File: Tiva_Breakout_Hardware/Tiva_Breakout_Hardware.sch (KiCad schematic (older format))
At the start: 6 parts, among them U1 TM4C129E_Launchpad

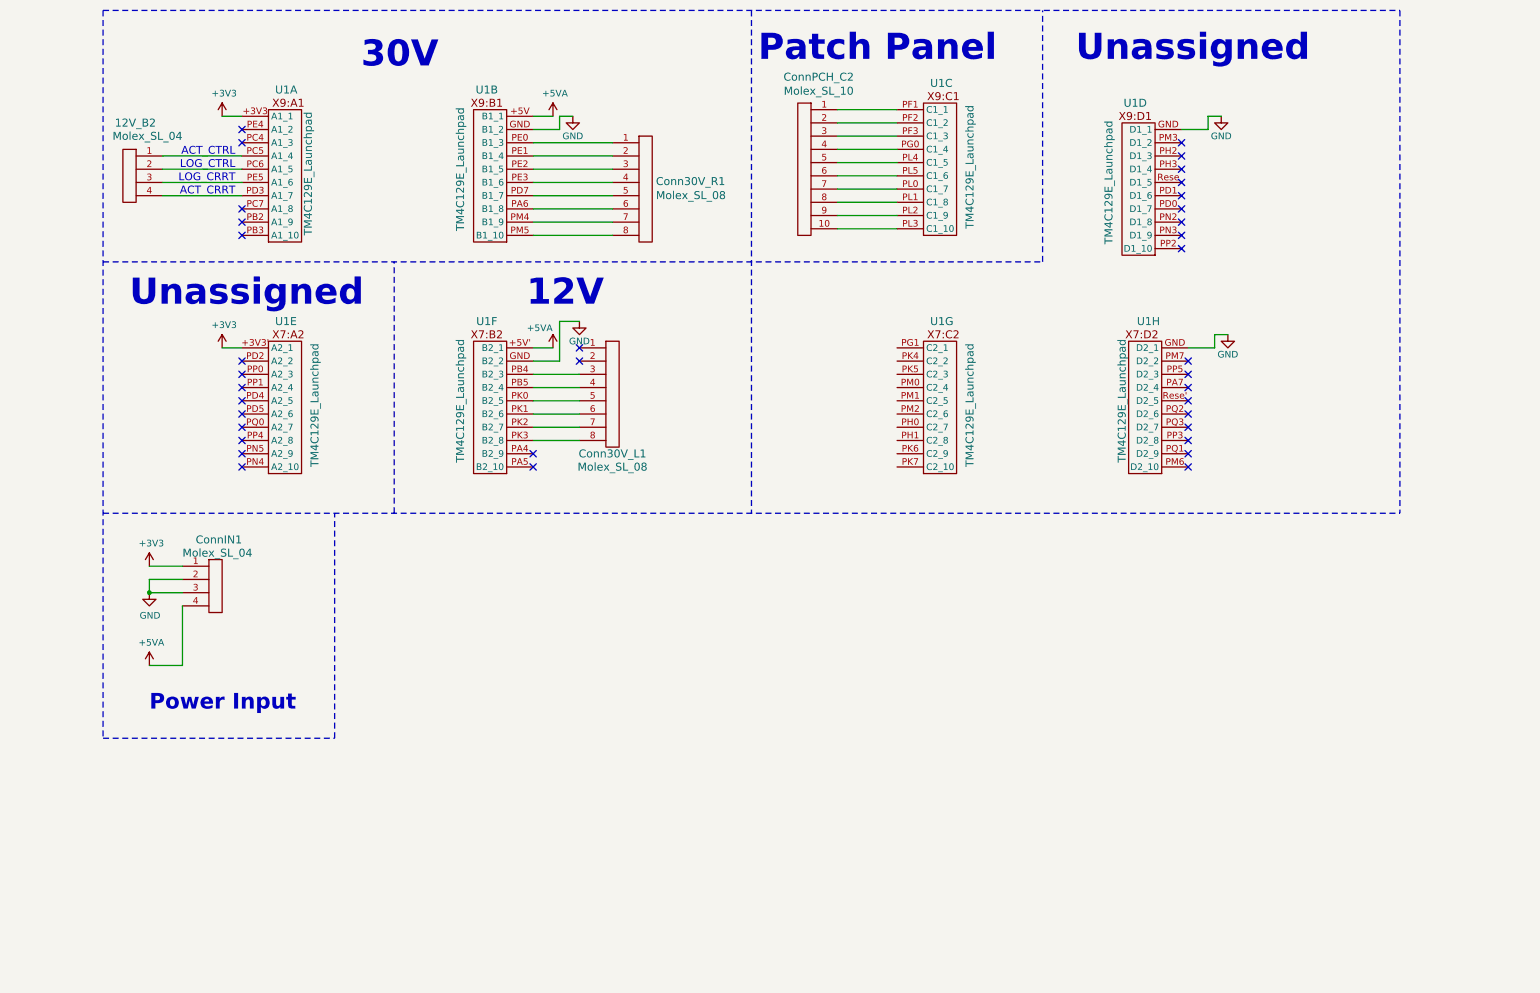
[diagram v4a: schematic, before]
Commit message: Corrected schematic to match 30V board
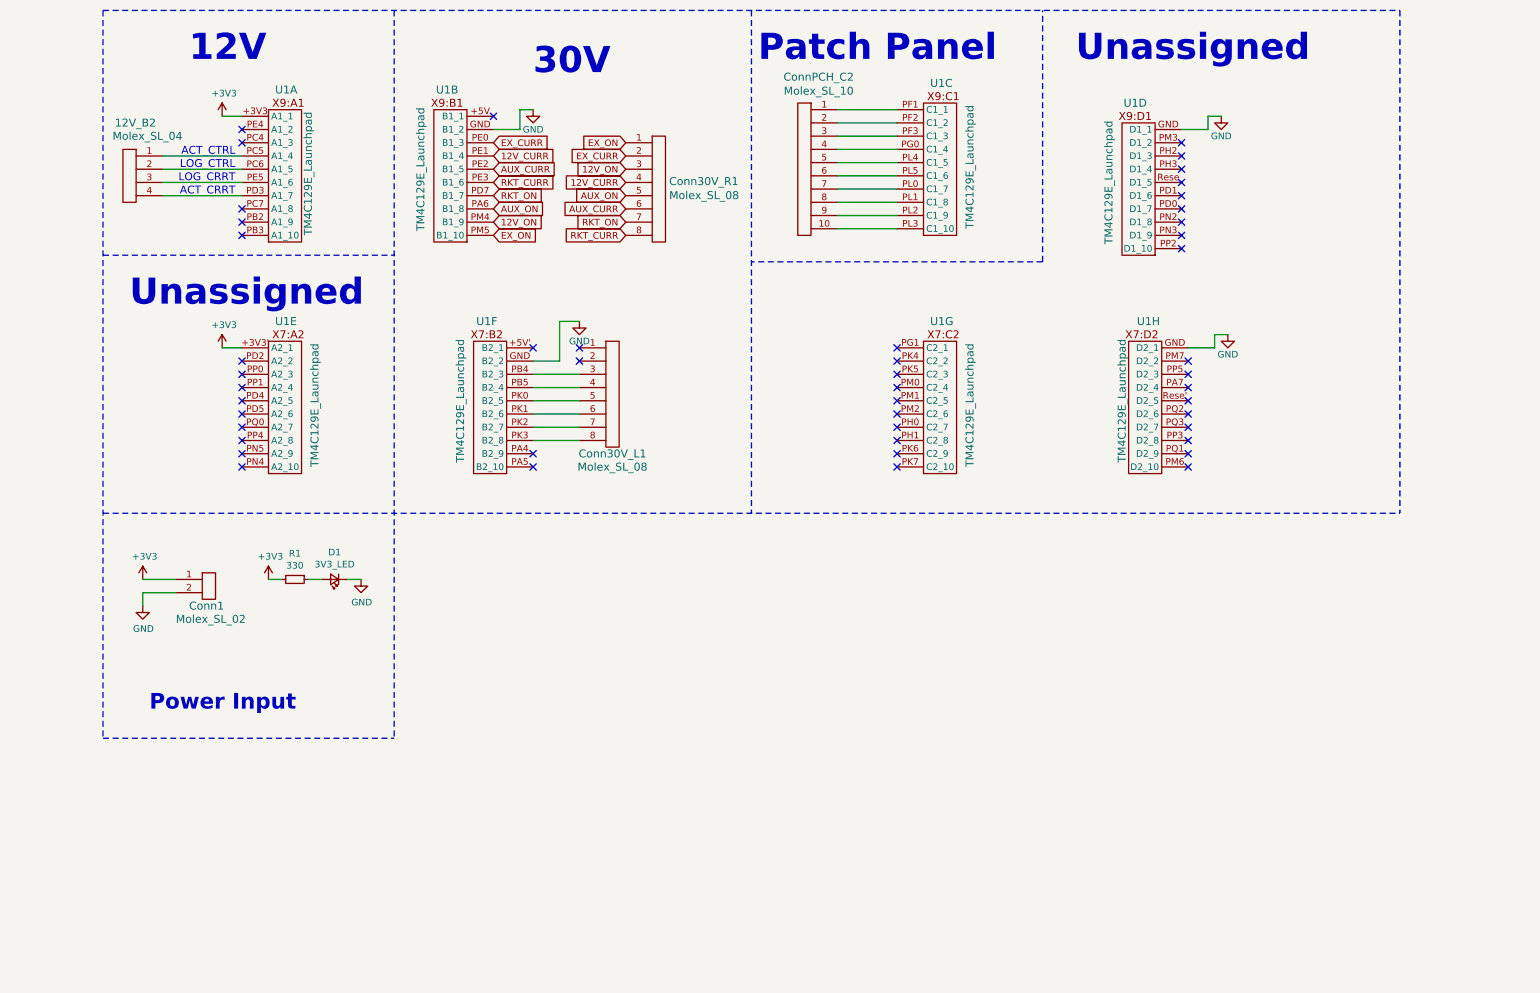
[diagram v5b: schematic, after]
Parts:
- removed ConnIN1: Molex_SL_04, MRDT_Connectors:MOLEX_SL_04_Horizontal, symbol Tiva_Breakout_Hardware-rescue:Molex_SL_04-MRDT_Connectors
- added Conn1: Molex_SL_02, MRDT_Connectors:MOLEX_SL_02_Horizontal, symbol MRDT_Connectors:Molex_SL_02
- added D1: 3V3_LED, LED_SMD:LED_0603_1608Metric_Pad1.05x0.95mm_HandSolder, symbol Device:LED_Small
- added R1: 330, Resistor_SMD:R_0603_1608Metric_Pad1.05x0.95mm_HandSolder, symbol Device:R_Small
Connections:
- net +3V3: now also Conn1.1, R1.2
- net GND: now also Conn1.2, D1.1 (K)
- net AUX_CURR: now reaches Conn30V_R1.6
- net AUX_CURR: now also U1.PE2 (B1_5); no longer U1.PA6 (B1_8)
- net AUX_ON: now reaches Conn30V_R1.5
- net AUX_ON: now also U1.PA6 (B1_8); no longer U1.PD7 (B1_7)
- net EX_CURR: now reaches U1.PE0 (B1_3)
- net EX_CURR: now also Conn30V_R1.2; no longer Conn30V_R1.1
- net 12V_CURR: now reaches U1.PE1 (B1_4)
- net 12V_CURR: now also Conn30V_R1.4; no longer Conn30V_R1.2
- net 12V_ON: now reaches Conn30V_R1.3
- net 12V_ON: now also U1.PM4 (B1_9); no longer U1.PE2 (B1_5)
- net RKT_CURR: now reaches U1.PE3 (B1_6)
- net RKT_CURR: now also Conn30V_R1.8; no longer Conn30V_R1.4
- net RKT_ON: now reaches Conn30V_R1.7
- net RKT_ON: now also U1.PD7 (B1_7); no longer U1.PM4 (B1_9)
- net EX_ON: now reaches U1.PM5 (B1_10)
- net EX_ON: now also Conn30V_R1.1; no longer Conn30V_R1.8
- net +5VA: no longer names the net of U1.+5V (B1_1)
- net +5VA: no longer U1.+5V' (B2_1)
- new net: D1.2 (A), R1.1
- no-connect marks 36 -> 48
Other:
- moved on the sheet: Conn30V_R1, U1B
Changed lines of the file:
@@
 L power:GND #PWR0101
 U 1 1 5D91D7D5
-P 800 4850
-F 0 "#PWR0101" H 800 4600 50  0001 C CNN
-F 1 "GND" H 805 4677 50  0000 C CNN
-F 2 "" H 800 4850 50  0001 C CNN
-F 3 "" H 800 4850 50  0001 C CNN
-	1    800  4850
-	1    0    0    -1
-$EndComp
-Wire Wire Line
-	1050 4850 800  4850
-Wire Wire Line
-	800  4850 800  4750
-Wire Wire Line
-	800  4750 1050 4750
-Connection ~ 800  4850
-$Comp
-L power:+5VA #PWR0102
-U 1 1 5D91FD34
-P 800 5400
-F 0 "#PWR0102" H 800 5250 50  0001 C CNN
-F 1 "+5VA" H 815 5573 50  0000 C CNN
-F 2 "" H 800 5400 50  0001 C CNN
-F 3 "" H 800 5400 50  0001 C CNN
-	1    800  5400
-	1    0    0    -1
-$EndComp
-Wire Wire Line
-	800  4650 1050 4650
+P 750 4950
+F 0 "#PWR0101" H 750 4700 50  0001 C CNN
+F 1 "GND" H 755 4777 50  0000 C CNN
+F 2 "" H 750 4950 50  0001 C CNN
+F 3 "" H 750 4950 50  0001 C CNN
+	1    750  4950
+	1    0    0    -1
+$EndComp
+Wire Wire Line
+	750  4950 750  4850
+Wire Wire Line
+	750  4850 1000 4850
 $Comp
 L power:+3V3 #PWR0103
 U 1 1 5D920B87
-P 800 4650
-F 0 "#PWR0103" H 800 4500 50  0001 C CNN
-F 1 "+3V3" H 815 4823 50  0000 C CNN
-F 2 "" H 800 4650 50  0001 C CNN
-F 3 "" H 800 4650 50  0001 C CNN
-	1    800  4650
-	1    0    0    -1
-$EndComp
-Wire Wire Line
-	1050 4950 1050 5400
-Wire Wire Line
-	1050 5400 800  5400
-Wire Notes Line
-	2200 5950 2200 4250
+P 750 4750
+F 0 "#PWR0103" H 750 4600 50  0001 C CNN
+F 1 "+3V3" H 765 4923 50  0000 C CNN
+F 2 "" H 750 4750 50  0001 C CNN
+F 3 "" H 750 4750 50  0001 C CNN
+	1    750  4750
+	1    0    0    -1
+$EndComp
 Text Notes 800  5750 0    118  ~ 24
 Power Input
 NoConn ~ 8650 3400
-$Comp
-L power:+5VA #PWR0104
-U 1 1 5D92EDF1
-P 3850 3000
-F 0 "#PWR0104" H 3850 2850 50  0001 C CNN
-F 1 "+5VA" H 3750 3150 50  0000 C CNN
-F 2 "" H 3850 3000 50  0001 C CNN
-F 3 "" H 3850 3000 50  0001 C CNN
-	1    3850 3000
-	1    0    0    -1
-$EndComp
-Wire Wire Line
-	3700 3000 3850 3000
 $Comp
 L power:+3V3 #PWR0105
@@
 	1350 1250 1500 1250
 Wire Wire Line
-	3900 1250 4000 1250
-Wire Wire Line
-	3900 1350 3900 1250
-Wire Wire Line
-	3700 1350 3900 1350
+	3600 1200 3700 1200
+Wire Wire Line
+	3400 1350 3600 1350
 $Comp
 L power:GND #PWR0107
 U 1 1 5D932528
-P 4000 1250
-F 0 "#PWR0107" H 4000 1000 50  0001 C CNN
-F 1 "GND" H 4000 1100 50  0000 C CNN
-F 2 "" H 4000 1250 50  0001 C CNN
-F 3 "" H 4000 1250 50  0001 C CNN
-	1    4000 1250
-	1    0    0    -1
-$EndComp
-Wire Wire Line
-	3700 1250 3850 1250
-$Comp
-L power:+5VA #PWR0108
-U 1 1 5D92E21C
-P 3850 1250
-F 0 "#PWR0108" H 3850 1100 50  0001 C CNN
-F 1 "+5VA" H 3865 1423 50  0000 C CNN
-F 2 "" H 3850 1250 50  0001 C CNN
-F 3 "" H 3850 1250 50  0001 C CNN
-	1    3850 1250
+P 3700 1200
+F 0 "#PWR0107" H 3700 950 50  0001 C CNN
+F 1 "GND" H 3700 1050 50  0000 C CNN
+F 2 "" H 3700 1200 50  0001 C CNN
+F 3 "" H 3700 1200 50  0001 C CNN
+	1    3700 1200
 	1    0    0    -1
 $EndComp
@@
 	8850 2900 8950 2900
 Wire Wire Line
-	3700 1450 4300 1450
-Wire Wire Line
-	3700 1550 4300 1550
-Wire Wire Line
-	3700 1650 4300 1650
-Wire Wire Line
-	3700 1750 4300 1750
-Wire Wire Line
-	3700 1850 4300 1850
-Wire Wire Line
-	3700 1950 4300 1950
-Wire Wire Line
 	6000 1200 6450 1200
 Wire Wire Line
@@
 L Tiva_Breakout_Hardware-rescue:TM4C129E_Launchpad-MRDT_Shields U1
 U 2 1 5D8F2703
-P 3500 2200
-F 0 "U1" H 3650 3350 60  0000 C CNN
-F 1 "TM4C129E_Launchpad" V 3850 2750 60  0000 C CNN
-F 2 "MRDT_Shields:Tiva_Breakout" H 3500 2200 60  0001 C CNN
-F 3 "" H 3500 2200 60  0001 C CNN
-	2    3500 2200
+P 3200 2200
+F 0 "U1" H 3350 3350 60  0000 C CNN
+F 1 "TM4C129E_Launchpad" V 3550 2750 60  0000 C CNN
+F 2 "MRDT_Shields:Tiva_Breakout" H 3200 2200 60  0001 C CNN
+F 3 "" H 3200 2200 60  0001 C CNN
+	2    3200 2200
 	-1   0    0    -1
 $EndComp
@@
 	8    8450 3950
 	-1   0    0    -1
-$EndComp
-$Comp
-L Tiva_Breakout_Hardware-rescue:Molex_SL_04-MRDT_Connectors ConnIN1
-U 1 1 5D9064E6
-P 1250 5000
-F 0 "ConnIN1" H 1150 5550 60  0000 L CNN
-F 1 "Molex_SL_04" H 1050 5450 60  0000 L CNN
-F 2 "MRDT_Connectors:MOLEX_SL_04_Horizontal" H 1250 5000 60  0001 C CNN
-F 3 "" H 1250 5000 60  0001 C CNN
-	1    1250 5000
-	1    0    0    -1
 $EndComp
 $Comp
@@
 	-1   0    0    -1
 $EndComp
-Text Notes 2400 900  0    197  ~ 39
+Text Notes 3700 950  0    197  ~ 39
 30V
-Text Notes 3650 2700 0    197  ~ 39
+Text Notes 1100 850  0    197  ~ 39
 12V
 Wire Wire Line
@@
 Text Notes 5400 850  0    197  ~ 39
 Patch Panel
-Wire Notes Line
-	2650 4250 2650 2350
 Text Notes 650  2700 0    197  ~ 39
 Unassigned
 Wire Notes Line
 	450  4250 10250 4250
-Wire Notes Line
-	450  5950 2200 5950
 Wire Notes Line
 	450  450  450  5950
@@
 Wire Notes Line
 	7550 2350 7550 450
-Wire Notes Line
-	450  2350 7550 2350
 Text Notes 7800 850  0    197  ~ 39
 Unassigned
@@
 L MRDT_Connectors:Molex_SL_08 Conn30V_R1
 U 1 1 5DCE5C02
-P 4500 2200
-F 0 "Conn30V_R1" H 4628 2658 60  0000 L CNN
-F 1 "Molex_SL_08" H 4628 2552 60  0000 L CNN
-F 2 "MRDT_Connectors:MOLEX_SL_08_Horizontal" H 4500 2500 60  0001 C CNN
-F 3 "" H 4500 2500 60  0001 C CNN
-	1    4500 2200
-	1    0    0    -1
-$EndComp
-Wire Wire Line
-	3700 2050 4300 2050
-Wire Wire Line
-	3700 2150 4300 2150
+P 4600 2200
+F 0 "Conn30V_R1" H 4728 2658 60  0000 L CNN
+F 1 "Molex_SL_08" H 4728 2552 60  0000 L CNN
+F 2 "MRDT_Connectors:MOLEX_SL_08_Horizontal" H 4600 2500 60  0001 C CNN
+F 3 "" H 4600 2500 60  0001 C CNN
+	1    4600 2200
+	1    0    0    -1
+$EndComp
 NoConn ~ 4050 3000
 NoConn ~ 4050 3100
@@
 Wire Wire Line
 	900  1550 1500 1550
+$Comp
+L Device:R_Small R1
+U 1 1 5DD79B1A
+P 1900 4750
+F 0 "R1" V 1704 4750 50  0000 C CNN
+F 1 "330" V 1795 4750 50  0000 C CNN
+F 2 "Resistor_SMD:R_0603_1608Metric_Pad1.05x0.95mm_HandSolder" H 1900 4750 50  0001 C CNN
+F 3 "~" H 1900 4750 50  0001 C CNN
+	1    1900 4750
+	0    1    1    0
+$EndComp
+$Comp
+L Device:LED_Small D1
+U 1 1 5DD80F85
+P 2200 4750
+F 0 "D1" H 2200 4545 50  0000 C CNN
+F 1 "3V3_LED" H 2200 4636 50  0000 C CNN
+F 2 "LED_SMD:LED_0603_1608Metric_Pad1.05x0.95mm_HandSolder" V 2200 4750 50  0001 C CNN
+F 3 "~" V 2200 4750 50  0001 C CNN
+	1    2200 4750
+	-1   0    0    1
+$EndComp
+Wire Wire Line
+	2000 4750 2100 4750
+$Comp
+L power:GND #PWR0112
+U 1 1 5DD86867
+P 2400 4750
+F 0 "#PWR0112" H 2400 4500 50  0001 C CNN
+F 1 "GND" H 2405 4577 50  0000 C CNN
+F 2 "" H 2400 4750 50  0001 C CNN
+F 3 "" H 2400 4750 50  0001 C CNN
+	1    2400 4750
+	1    0    0    -1
+$EndComp
+Wire Wire Line
+	2300 4750 2400 4750
+$Comp
+L MRDT_Connectors:Molex_SL_02 Conn1
+U 1 1 5DD89AFE
+P 1200 4900
+F 0 "Conn1" H 1100 4850 60  0000 L CNN
+F 1 "Molex_SL_02" H 1000 4750 60  0000 L CNN
+F 2 "MRDT_Connectors:MOLEX_SL_02_Horizontal" H 1200 4800 60  0001 C CNN
+F 3 "" H 1200 4800 60  0001 C CNN
+	1    1200 4900
+	1    0    0    -1
+$EndComp
+NoConn ~ 3700 3000
+NoConn ~ 3400 1250
+NoConn ~ 6450 3000
+NoConn ~ 6450 3100
+NoConn ~ 6450 3200
+NoConn ~ 6450 3300
+NoConn ~ 6450 3400
+NoConn ~ 6450 3500
+NoConn ~ 6450 3600
+NoConn ~ 6450 3700
+NoConn ~ 6450 3800
+NoConn ~ 6450 3900
+Wire Notes Line
+	450  2300 2650 2300
+Wire Notes Line
+	7550 2350 5350 2350
+Wire Wire Line
+	3600 1200 3600 1350
+Text GLabel 3400 1450 2    50   Input ~ 0
+EX_CURR
+Text GLabel 3400 1550 2    50   Input ~ 0
+12V_CURR
+Text GLabel 3400 1650 2    50   Input ~ 0
+AUX_CURR
+Text GLabel 3400 1750 2    50   Input ~ 0
+RKT_CURR
+Text GLabel 3400 1850 2    50   Input ~ 0
+RKT_ON
+Text GLabel 3400 1950 2    50   Input ~ 0
+AUX_ON
+Text GLabel 3400 2050 2    50   Input ~ 0
+12V_ON
+Text GLabel 3400 2150 2    50   Input ~ 0
+EX_ON
+Text GLabel 4400 1450 0    50   Input ~ 0
+EX_ON
+Text GLabel 4400 1550 0    50   Input ~ 0
+EX_CURR
+Text GLabel 4400 1650 0    50   Input ~ 0
+12V_ON
+Text GLabel 4400 1750 0    50   Input ~ 0
+12V_CURR
+Text GLabel 4400 1850 0    50   Input ~ 0
+AUX_ON
+Text GLabel 4400 1950 0    50   Input ~ 0
+AUX_CURR
+Text GLabel 4400 2050 0    50   Input ~ 0
+RKT_ON
+Text GLabel 4400 2150 0    50   Input ~ 0
+RKT_CURR
+Wire Notes Line
+	2650 450  2650 5950
+Wire Notes Line
+	450  5950 2650 5950
+Wire Wire Line
+	750  4750 1000 4750
+$Comp
+L power:+3V3 #PWR?
+U 1 1 5DDB7870
+P 1700 4750
+F 0 "#PWR?" H 1700 4600 50  0001 C CNN
+F 1 "+3V3" H 1715 4923 50  0000 C CNN
+F 2 "" H 1700 4750 50  0001 C CNN
+F 3 "" H 1700 4750 50  0001 C CNN
+	1    1700 4750
+	1    0    0    -1
+$EndComp
+Wire Wire Line
+	1700 4750 1800 4750
 $EndSCHEMATC

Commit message: Ready for CDR
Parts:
- Conn30V_L1: value Molex_SL_08 -> Molex_SL_07; footprint MRDT_Connectors:MOLEX_SL_08_Horizontal -> MRDT_Connectors:MOLEX_SL_07_Horizontal; symbol MRDT_Connectors:Molex_SL_08 -> MRDT_Connectors:Molex_SL_07
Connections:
- net +3V3: now also Conn1.2; no longer Conn1.1
- net GND: now also Conn1.1; no longer Conn1.2
- net at U1.PB4 (B2_3): now also Conn30V_L1.2; no longer Conn30V_L1.3
- net at U1.PB5 (B2_4): now also Conn30V_L1.3; no longer Conn30V_L1.4
- net at U1.PK0 (B2_5): now also Conn30V_L1.4; no longer Conn30V_L1.5
- net at U1.PK1 (B2_6): now also Conn30V_L1.5; no longer Conn30V_L1.6
- net at U1.PK2 (B2_7): now also Conn30V_L1.6; no longer Conn30V_L1.7
- net at U1.PK3 (B2_8): now also Conn30V_L1.7; no longer Conn30V_L1.8
- no-connect marks 48 -> 47
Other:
- moved on the sheet: Conn1
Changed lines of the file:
@@
 L power:GND #PWR0101
 U 1 1 5D91D7D5
-P 750 4950
-F 0 "#PWR0101" H 750 4700 50  0001 C CNN
-F 1 "GND" H 755 4777 50  0000 C CNN
-F 2 "" H 750 4950 50  0001 C CNN
-F 3 "" H 750 4950 50  0001 C CNN
-	1    750  4950
-	1    0    0    -1
-$EndComp
-Wire Wire Line
-	750  4950 750  4850
-Wire Wire Line
-	750  4850 1000 4850
+P 750 4800
+F 0 "#PWR0101" H 750 4550 50  0001 C CNN
+F 1 "GND" H 755 4627 50  0000 C CNN
+F 2 "" H 750 4800 50  0001 C CNN
+F 3 "" H 750 4800 50  0001 C CNN
+	1    750  4800
+	1    0    0    -1
+$EndComp
+Wire Wire Line
+	750  4800 750  4700
+Wire Wire Line
+	750  4700 1000 4700
 $Comp
 L power:+3V3 #PWR0103
 U 1 1 5D920B87
-P 750 4750
-F 0 "#PWR0103" H 750 4600 50  0001 C CNN
-F 1 "+3V3" H 765 4923 50  0000 C CNN
-F 2 "" H 750 4750 50  0001 C CNN
-F 3 "" H 750 4750 50  0001 C CNN
-	1    750  4750
+P 750 4600
+F 0 "#PWR0103" H 750 4450 50  0001 C CNN
+F 1 "+3V3" H 765 4773 50  0000 C CNN
+F 2 "" H 750 4600 50  0001 C CNN
+F 3 "" H 750 4600 50  0001 C CNN
+	1    750  4600
 	1    0    0    -1
 $EndComp
@@
 	3700 3700 4050 3700
 $Comp
-L MRDT_Connectors:Molex_SL_08 Conn30V_L1
+L MRDT_Connectors:Molex_SL_07 Conn30V_L1
 U 1 1 5DCE1DDF
 P 4250 3750
 F 0 "Conn30V_L1" H 4300 3700 60  0000 C CNN
-F 1 "Molex_SL_08" H 4300 3600 60  0000 C CNN
-F 2 "MRDT_Connectors:MOLEX_SL_08_Horizontal" H 4250 4050 60  0001 C CNN
+F 1 "Molex_SL_07" H 4300 3600 60  0000 C CNN
+F 2 "MRDT_Connectors:MOLEX_SL_07_Horizontal" H 4250 4050 60  0001 C CNN
 F 3 "" H 4250 4050 60  0001 C CNN
 	1    4250 3750
@@
 	1    0    0    -1
 $EndComp
-NoConn ~ 4050 3000
 NoConn ~ 4050 3100
 Wire Wire Line
@@
 L MRDT_Connectors:Molex_SL_02 Conn1
 U 1 1 5DD89AFE
-P 1200 4900
-F 0 "Conn1" H 1100 4850 60  0000 L CNN
-F 1 "Molex_SL_02" H 1000 4750 60  0000 L CNN
-F 2 "MRDT_Connectors:MOLEX_SL_02_Horizontal" H 1200 4800 60  0001 C CNN
-F 3 "" H 1200 4800 60  0001 C CNN
-	1    1200 4900
-	1    0    0    -1
+P 1200 4550
+F 0 "Conn1" H 1100 4500 60  0000 L CNN
+F 1 "Molex_SL_02" H 1000 4400 60  0000 L CNN
+F 2 "MRDT_Connectors:MOLEX_SL_02_Horizontal" H 1200 4450 60  0001 C CNN
+F 3 "" H 1200 4450 60  0001 C CNN
+	1    1200 4550
+	1    0    0    1
 $EndComp
 NoConn ~ 3700 3000
@@
 	450  5950 2650 5950
 Wire Wire Line
-	750  4750 1000 4750
-$Comp
-L power:+3V3 #PWR?
+	750  4600 1000 4600
+$Comp
+L power:+3V3 #PWR0102
 U 1 1 5DDB7870
 P 1700 4750
-F 0 "#PWR?" H 1700 4600 50  0001 C CNN
+F 0 "#PWR0102" H 1700 4600 50  0001 C CNN
 F 1 "+3V3" H 1715 4923 50  0000 C CNN
 F 2 "" H 1700 4750 50  0001 C CNN
